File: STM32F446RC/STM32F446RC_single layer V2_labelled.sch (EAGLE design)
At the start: 75 parts, among them IC1 STM32F446RCT6

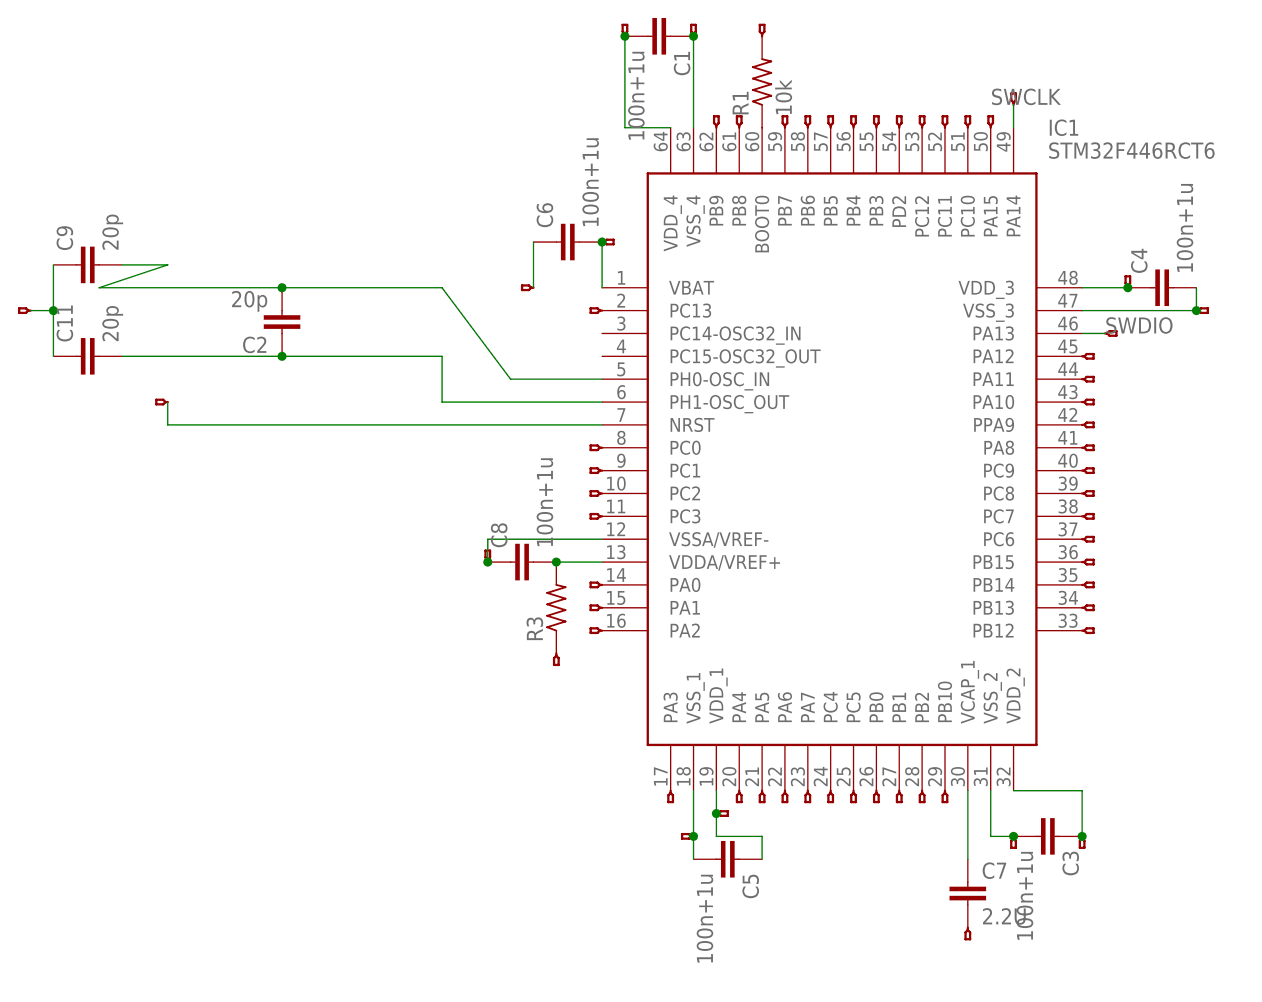
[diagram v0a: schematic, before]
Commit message: added double layer
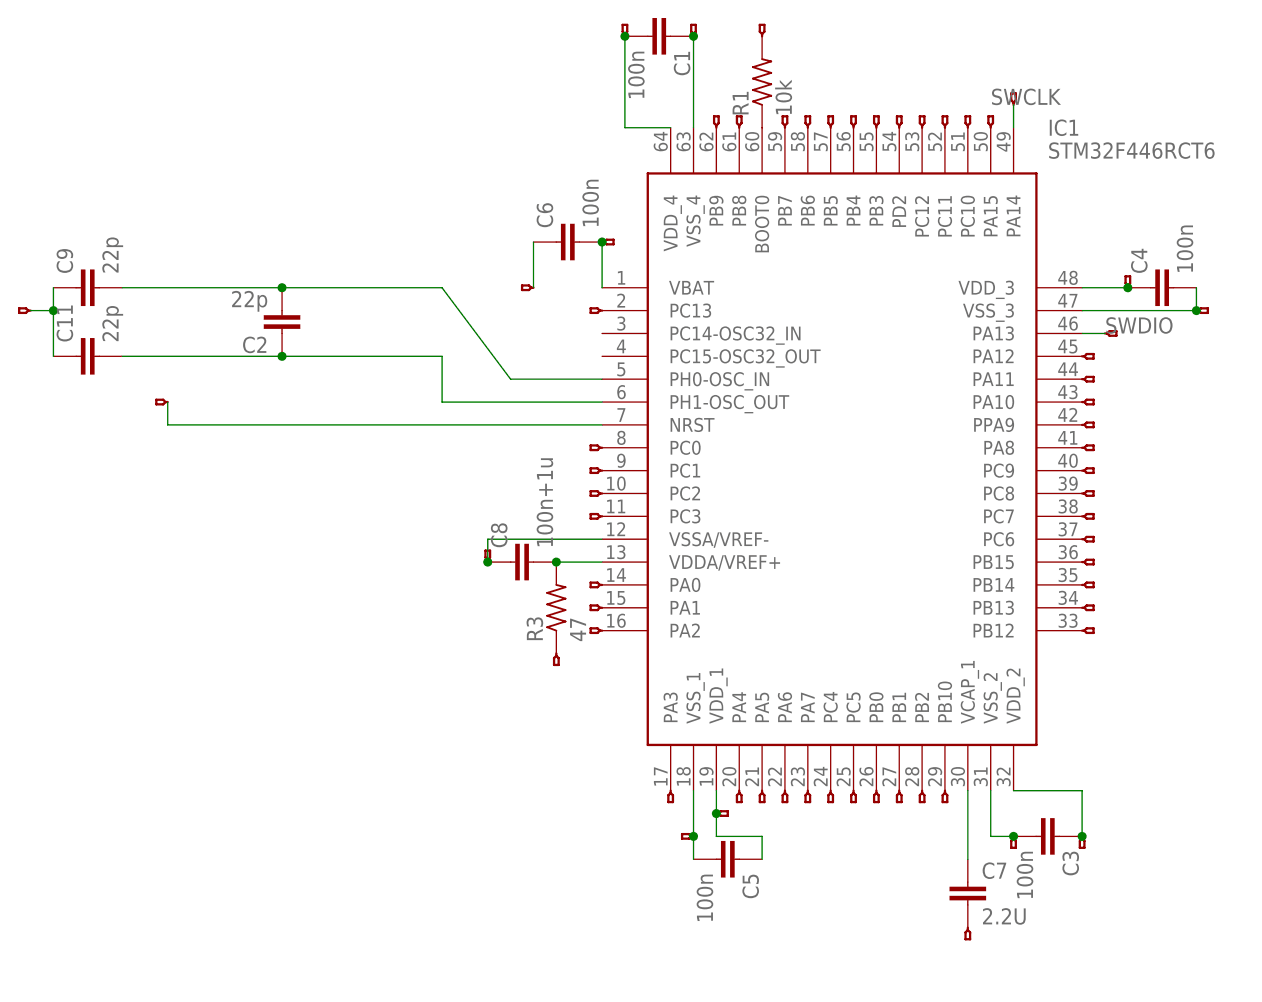
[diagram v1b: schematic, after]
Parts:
- C1, C3, C4, C5, C6: value 100n+1u -> 100n
- C11, C2, C9: value 20p -> 22p
- R3: value (none) -> 47
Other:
- moved on the sheet: C9
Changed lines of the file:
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@@
 <part name="IC1" library="STM32F446RCT6" deviceset="STM32F446RCT6" device=""/>
 <part name="R1" library="rcl" library_urn="urn:adsk.eagle:library:334" deviceset="R-US_" device="0204/2V" package3d_urn="urn:adsk.eagle:package:23495/1" value="10k"/>
-<part name="C1" library="capacitor-wima" library_urn="urn:adsk.eagle:library:116" deviceset="C" device="2,5-3" package3d_urn="urn:adsk.eagle:package:5436/1" value="100n+1u"/>
-<part name="C3" library="capacitor-wima" library_urn="urn:adsk.eagle:library:116" deviceset="C" device="2,5-3" package3d_urn="urn:adsk.eagle:package:5436/1" value="100n+1u"/>
-<part name="C4" library="capacitor-wima" library_urn="urn:adsk.eagle:library:116" deviceset="C" device="2,5-3" package3d_urn="urn:adsk.eagle:package:5436/1" value="100n+1u"/>
-<part name="C5" library="capacitor-wima" library_urn="urn:adsk.eagle:library:116" deviceset="C" device="2,5-3" package3d_urn="urn:adsk.eagle:package:5436/1" value="100n+1u"/>
-<part name="R3" library="rcl" library_urn="urn:adsk.eagle:library:334" deviceset="R-US_" device="0204/2V" package3d_urn="urn:adsk.eagle:package:23495/1"/>
-<part name="C6" library="capacitor-wima" library_urn="urn:adsk.eagle:library:116" deviceset="C" device="2,5-3" package3d_urn="urn:adsk.eagle:package:5436/1" value="100n+1u"/>
+<part name="C1" library="capacitor-wima" library_urn="urn:adsk.eagle:library:116" deviceset="C" device="2,5-3" package3d_urn="urn:adsk.eagle:package:5436/1" value="100n"/>
+<part name="C3" library="capacitor-wima" library_urn="urn:adsk.eagle:library:116" deviceset="C" device="2,5-3" package3d_urn="urn:adsk.eagle:package:5436/1" value="100n"/>
+<part name="C4" library="capacitor-wima" library_urn="urn:adsk.eagle:library:116" deviceset="C" device="2,5-3" package3d_urn="urn:adsk.eagle:package:5436/1" value="100n"/>
+<part name="C5" library="capacitor-wima" library_urn="urn:adsk.eagle:library:116" deviceset="C" device="2,5-3" package3d_urn="urn:adsk.eagle:package:5436/1" value="100n"/>
+<part name="R3" library="rcl" library_urn="urn:adsk.eagle:library:334" deviceset="R-US_" device="0204/2V" package3d_urn="urn:adsk.eagle:package:23495/1" value="47"/>
+<part name="C6" library="capacitor-wima" library_urn="urn:adsk.eagle:library:116" deviceset="C" device="2,5-3" package3d_urn="urn:adsk.eagle:package:5436/1" value="100n"/>
 <part name="C7" library="capacitor-wima" library_urn="urn:adsk.eagle:library:116" deviceset="C" device="2,5-3" package3d_urn="urn:adsk.eagle:package:5436/1" value="2.2U"/>
 <part name="C8" library="capacitor-wima" library_urn="urn:adsk.eagle:library:116" deviceset="C" device="2,5-3" package3d_urn="urn:adsk.eagle:package:5436/1" value="100n+1u"/>
-<part name="C9" library="capacitor-wima" library_urn="urn:adsk.eagle:library:116" deviceset="C" device="2,5-3" package3d_urn="urn:adsk.eagle:package:5436/1" value="20p"/>
-<part name="C11" library="capacitor-wima" library_urn="urn:adsk.eagle:library:116" deviceset="C" device="2,5-3" package3d_urn="urn:adsk.eagle:package:5436/1" value="20p"/>
+<part name="C9" library="capacitor-wima" library_urn="urn:adsk.eagle:library:116" deviceset="C" device="2,5-3" package3d_urn="urn:adsk.eagle:package:5436/1" value="22p"/>
+<part name="C11" library="capacitor-wima" library_urn="urn:adsk.eagle:library:116" deviceset="C" device="2,5-3" package3d_urn="urn:adsk.eagle:package:5436/1" value="22p"/>
 <part name="JP3" library="F405Pill" deviceset="HEADERHOLE" device="-HEADERHOLE"/>
 <part name="JP4" library="F405Pill" deviceset="HEADERHOLE" device="-HEADERHOLE"/>
@@
 <part name="JP65" library="F405Pill" deviceset="HEADERHOLE" device="-HEADERHOLE"/>
 <part name="JP7" library="F405Pill" deviceset="HEADERHOLE" device="-HEADERHOLE"/>
-<part name="C2" library="capacitor-wima" library_urn="urn:adsk.eagle:library:116" deviceset="C" device="2,5-3" package3d_urn="urn:adsk.eagle:package:5436/1" value="20p"/>
+<part name="C2" library="capacitor-wima" library_urn="urn:adsk.eagle:library:116" deviceset="C" device="2,5-3" package3d_urn="urn:adsk.eagle:package:5436/1" value="22p"/>
 </parts>
 <sheets>
@@
 <attribute name="VALUE" x="25.019" y="34.544" size="1.778" layer="96" rot="R90"/>
 </instance>
-<instance part="C9" gate="G$1" x="-27.94" y="66.04" rot="R90">
-<attribute name="NAME" x="-28.321" y="67.564" size="1.778" layer="95" rot="R90"/>
-<attribute name="VALUE" x="-23.241" y="67.564" size="1.778" layer="96" rot="R90"/>
+<instance part="C9" gate="G$1" x="-27.94" y="63.5" rot="R90">
+<attribute name="NAME" x="-28.321" y="65.024" size="1.778" layer="95" rot="R90"/>
+<attribute name="VALUE" x="-23.241" y="65.024" size="1.778" layer="96" rot="R90"/>
 </instance>
 <instance part="C11" gate="G$1" x="-27.94" y="55.88" rot="R90">
@@
 <net name="N$7" class="0">
 <segment>
-<pinref part="C11" gate="G$1" pin="2"/>
 <pinref part="IC1" gate="G$1" pin="PH1-OSC_OUT"/>
 <wire x1="30.48" y1="50.8" x2="12.7" y2="50.8" width="0.1524" layer="91"/>
 <wire x1="12.7" y1="50.8" x2="12.7" y2="55.88" width="0.1524" layer="91"/>
-<wire x1="-22.86" y1="55.88" x2="-5.08" y2="55.88" width="0.1524" layer="91"/>
 <pinref part="C2" gate="G$1" pin="1"/>
 <wire x1="-5.08" y1="55.88" x2="12.7" y2="55.88" width="0.1524" layer="91"/>
+<pinref part="C11" gate="G$1" pin="2"/>
+<wire x1="-5.08" y1="55.88" x2="-22.86" y2="55.88" width="0.1524" layer="91"/>
 <junction x="-5.08" y="55.88"/>
 </segment>
@@
 <net name="N$53" class="0">
 <segment>
-<pinref part="C9" gate="G$1" pin="2"/>
-<wire x1="-17.78" y1="66.04" x2="-22.86" y2="66.04" width="0.1524" layer="91"/>
 <pinref part="IC1" gate="G$1" pin="PH0-OSC_IN"/>
 <wire x1="30.48" y1="53.34" x2="20.32" y2="53.34" width="0.1524" layer="91"/>
 <wire x1="20.32" y1="53.34" x2="12.7" y2="63.5" width="0.1524" layer="91"/>
+<pinref part="C2" gate="G$1" pin="2"/>
 <wire x1="12.7" y1="63.5" x2="-5.08" y2="63.5" width="0.1524" layer="91"/>
-<wire x1="-5.08" y1="63.5" x2="-25.4" y2="63.5" width="0.1524" layer="91"/>
-<wire x1="-17.78" y1="66.04" x2="-25.4" y2="63.5" width="0.1524" layer="91"/>
-<pinref part="C2" gate="G$1" pin="2"/>
+<pinref part="C9" gate="G$1" pin="2"/>
+<wire x1="-5.08" y1="63.5" x2="-22.86" y2="63.5" width="0.1524" layer="91"/>
 <junction x="-5.08" y="63.5"/>
 </segment>
@@
 <pinref part="C9" gate="G$1" pin="1"/>
 <wire x1="-30.48" y1="55.88" x2="-30.48" y2="60.96" width="0.1524" layer="91"/>
-<wire x1="-30.48" y1="60.96" x2="-30.48" y2="66.04" width="0.1524" layer="91"/>
+<wire x1="-30.48" y1="60.96" x2="-30.48" y2="63.5" width="0.1524" layer="91"/>
 <wire x1="-30.48" y1="60.96" x2="-33.02" y2="60.96" width="0.1524" layer="91"/>
 <junction x="-30.48" y="60.96"/>
